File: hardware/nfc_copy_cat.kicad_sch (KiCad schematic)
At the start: 38 parts, among them J1 USB_B_Micro, J2 Battery, J3 NFC Module V3, J4 Adafruit NFC 1.0, J5 Conn_01x02, J6 SWD, SW1 ON/OFF, SW2 RST, SW3 Magspoof, SW4 NFC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

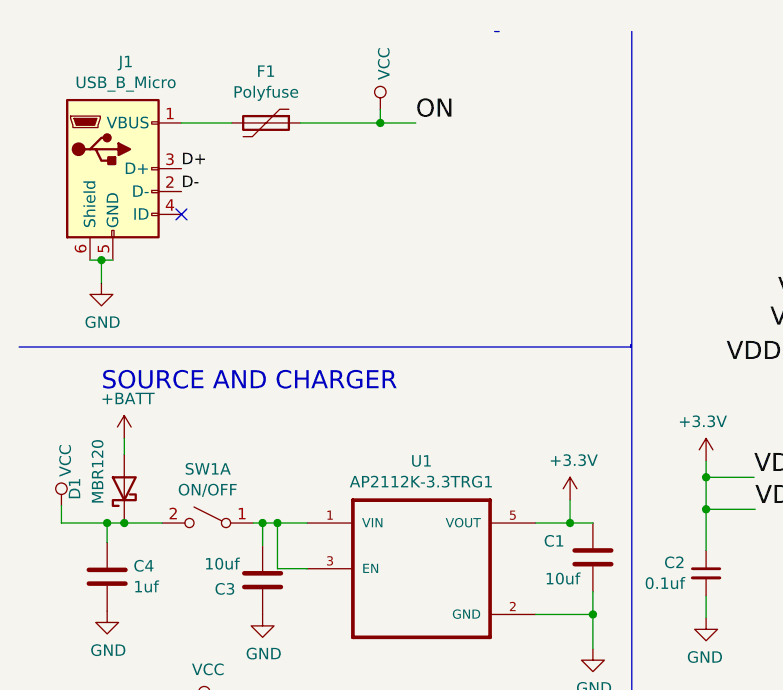
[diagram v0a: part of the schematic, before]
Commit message: Add labels and change ON
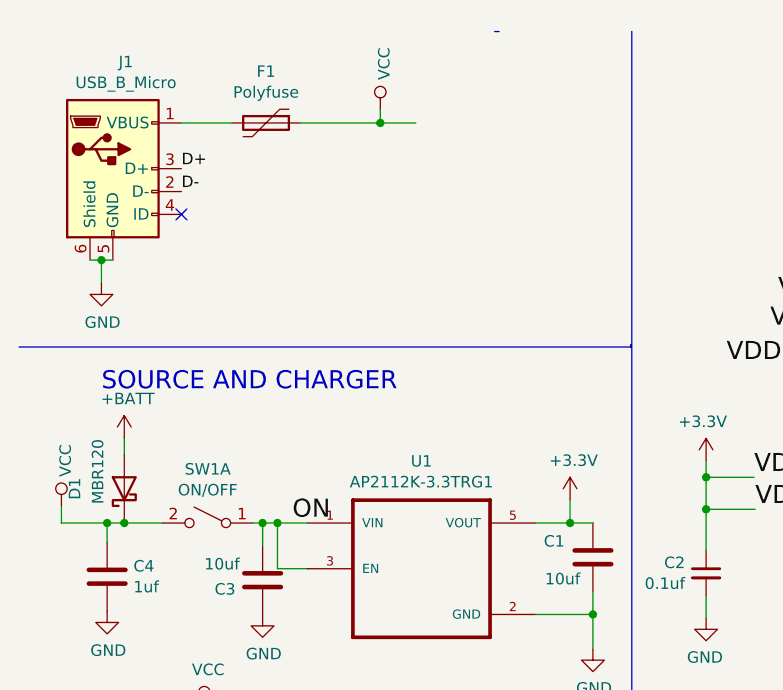
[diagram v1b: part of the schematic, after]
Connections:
- net VCC: no longer D3.2 (A)
- net ON: now reaches C3.1, SW1.1 (A), U1.1 (VIN), U1.3 (EN)
- net ON: now also D3.2 (A)
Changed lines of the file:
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@@
     (effects (font (size 1.27 1.27)) (justify right bottom))
   )
-  (label "ON" (at 56.007 22.352 0)
+  (label "ON" (at 42.291 66.802 0)
     (effects (font (size 2.0066 2.0066)) (justify left bottom))
   )
